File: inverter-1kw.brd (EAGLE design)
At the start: 96.4 x 87.3 mm, 240 parts, among them IC1 LMV358MMX, IC2 LMV358MMX, U1 ACS712, U4 ACS712, U5 SI8230, U6 SI8230, U7 ACS712, X1 GMSTBV3, X2 MSTBV2

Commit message: planler yapıldı tekrar
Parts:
- moved R44 77.4 mm to (20.4, 15.6)
- moved C2 10.7 mm to (29.7, 38.7)
- moved C7 7.79 mm to (35.6, 27.3)
- moved C3 7.74 mm to (35.5, 32.6)
- moved C5 7.62 mm to (35.5, 29.9)
- moved TP20 2.01 mm to (41.2, 18.7)
- moved R7 1.18 mm to (35.9, 22.2)
- moved R6 1.16 mm to (38.9, 22.2)
- moved R5 1.14 mm to (41.9, 22.2)
- moved R74 0.48 mm to (6.38, 62.2)
- moved R72 0.47 mm to (9.11, 62.2)
- moved R68 0.45 mm to (9.93, 66.5)
- moved R2 0.42 mm to (38.8, 16.6)
- moved R3 0.41 mm to (35.8, 16.6)
- moved R1 0.38 mm to (41.9, 16.6)
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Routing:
- net VB_FILTER: track 26.2 -> 2.54 mm
- net VA_OUT: track 18.9 -> 1.30 mm
- net VG1_P: track 14.8 -> 26.8 mm, vias 0 -> 2
- net VIN: track 27.8 -> 21.7 mm, vias 12 -> 18
- net AGND: track 93.0 -> 86.9 mm, vias 56 -> 54
- net DGND: track 146.7 -> 148.6 mm, vias 16 -> 17
- net N$79: track 7.63 -> 6.63 mm
- net SW_LEG_A: track 24.4 -> 24.1 mm, vias 6 -> 20
- net VB_OUT: vias 1 -> 9
- net SW_LEG_B: vias 6 -> 7
- added copper zone on layer 1, net SW_LEG_B
- added copper zone on layer 16, net VB_FILTER

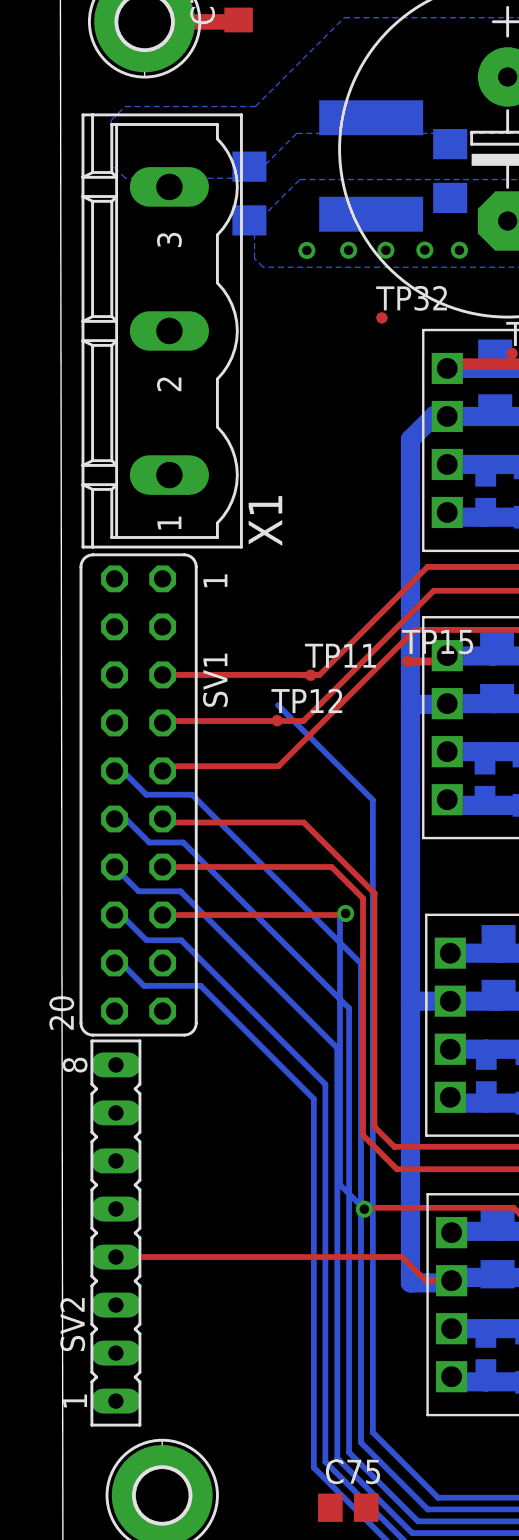
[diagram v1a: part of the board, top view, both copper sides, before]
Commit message: Kontrol karti soketi SMD yapildi, guc giris soketi ve guc-karti soketi bottom-layer'a alindi.
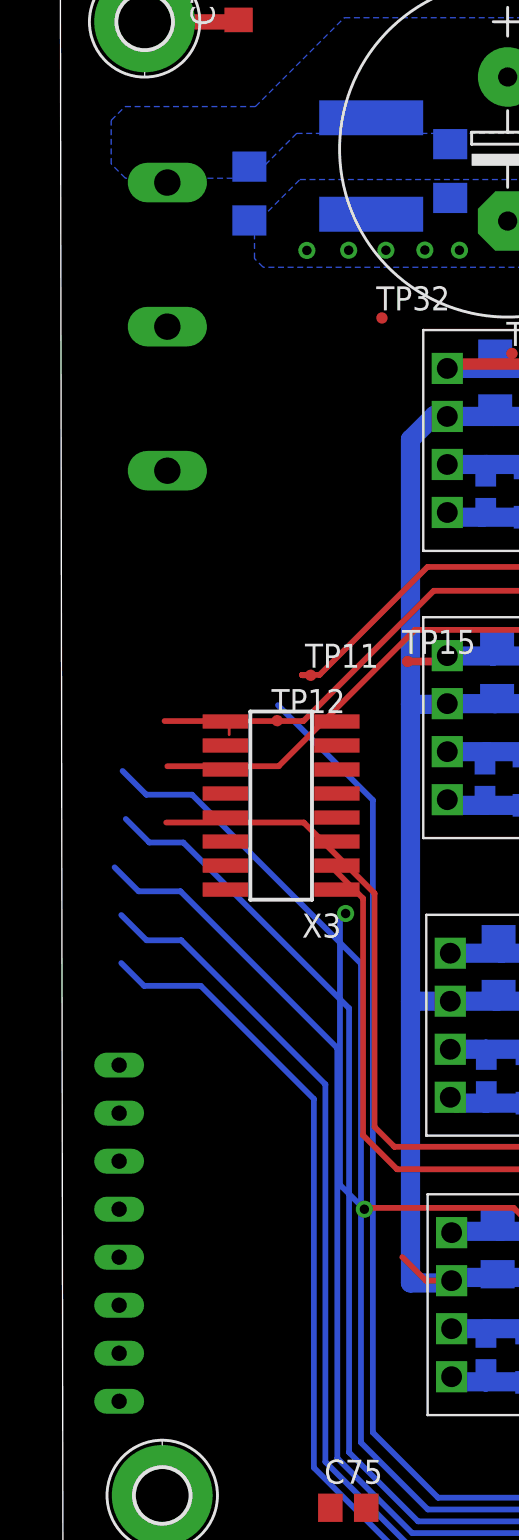
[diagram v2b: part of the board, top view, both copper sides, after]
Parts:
- removed SV1: (no value), con-lsta:FE10-2
- added X3: 1365-16, con-leotronics:1365-16
- moved X1 0.25 mm to (-26.4, 75.3), flipped to the bottom, turned to 270 degrees
- moved SV2 0.17 mm to (-29.0, 27.4), flipped to the bottom
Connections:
- removed net N$38: SV1.8
- removed net RELAY1: SV1.2
- removed net RELAY2: SV1.4
- net +3V3: now also X3.2; no longer SV1.17
- net +5V: no longer SV1.19
- net DGND: now also X3.1; no longer SV1.20
- net DRV1_EN: now also X3.9; no longer SV1.9
- net DRV2_EN: now also X3.3; no longer SV1.15
- net G11_PWM: now also X3.13; no longer SV1.5
- net G12_PWM: now also X3.11; no longer SV1.7
- net G13_PWM: now also X3.7; no longer SV1.11
- net G14_PWM: now also X3.5; no longer SV1.13
- net IA_SENS: now also X3.8; no longer SV1.14
- net IB_SENS: now also X3.4; no longer SV1.18
- net IIN_SENS: now also X3.15; no longer SV1.3
- net VA_SENS: now also X3.10; no longer SV1.12
- net VB_SENS: now also X3.6; no longer SV1.16
- net VIN_SENS: now also X3.16; no longer SV1.1
- net VIN_SENS_DIFF: now also X3.14; no longer SV1.6
- net VOUT_SENS_DIFF: now also X3.12; no longer SV1.10
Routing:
- net PE: track 1.94 -> 17.3 mm
- net VDD: track 93.5 -> 78.4 mm
- net DRV2_EN: track 48.7 -> 39.1 mm
- net G14_PWM: track 43.7 -> 34.8 mm
- net G11_PWM: track 33.6 -> 26.3 mm
- net G12_PWM: track 32.6 -> 33.3 mm
- net VA_SENS: track 164.0 -> 163.4 mm

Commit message: Planeler tamamlandı.
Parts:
- moved TP32 76.9 mm to (61.7, 71.7)
- moved TP14 39.5 mm to (31.8, 22.6)
- moved TP11 38.3 mm to (16.0, 41.1)
- moved TP12 38.0 mm to (14.4, 39.7)
- moved TP21 33.7 mm to (80.3, 15.2)
- moved SV2 33.6 mm to (4.12, 21.7)
- moved C76 33.5 mm to (9.51, 83.1), turned to 270 degrees
- moved TP28 33.3 mm to (33.4, 62.1)
- moved C10 33.2 mm to (87.5, 21.6)
- moved R21 33.2 mm to (85.5, 21.6)
- moved C13 33.2 mm to (74.5, 12.1)
- moved C15 33.2 mm to (74.5, 8.65)
- moved C17 33.2 mm to (87.5, 56.2)
- moved C38 33.2 mm to (78.0, 6.36)
- moved C5 33.2 mm to (67.5, 21.2)
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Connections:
- net PE: now also X1.3; no longer X1.1
- net VSUPPLY+: now also X1.1; no longer X1.3
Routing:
- net +3V3: track 7.94 -> 273.1 mm, vias 1 -> 8
- net PE: track 17.3 -> 259.8 mm, vias 0 -> 1
- net VIN_SENS: track 2.23 -> 84.4 mm, vias 0 -> 1
- net AGND: track 86.9 -> 153.7 mm, vias 54 -> 62
- net IIN_SENS: track 6.73 -> 39.3 mm
- net VDD: track 78.4 -> 92.8 mm
- net G13_PWM: track 46.2 -> 33.5 mm
- net G11_PWM: track 26.3 -> 35.9 mm
- net N$42: track 0.00 -> 6.64 mm
- net VB_OUT: track 7.85 -> 14.4 mm
- net VA_OUT: track 1.30 -> 7.68 mm, vias 0 -> 1
- net VB_SENS: track 153.6 -> 159.3 mm, vias 2 -> 4
- net N$41: track 0.00 -> 5.35 mm
- net VOUT_SENS_DIFF: track 130.1 -> 125.8 mm, vias 1 -> 2
- net IB_SENS: track 140.3 -> 144.3 mm, vias 1 -> 2
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- added copper zone on layer 15, net +5V

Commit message: İyileştirmeler yapıldı
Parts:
- moved C8 6.51 mm to (67.4, 59.2)
- moved C4 6.51 mm to (67.4, 64.9)
- moved C6 6.51 mm to (67.4, 61.9)
- moved TP34 5.56 mm to (18.3, 64.7)
- moved TP33 5.23 mm to (33.1, 69.2), turned to 90 degrees
- moved C1 2.31 mm to (61.8, 52.7)
- moved TP22 1.01 mm to (86.1, 5.34)
- moved TP14 0.61 mm to (32.1, 23.1)
- moved TP5 0.60 mm to (45.1, 54.1)
- moved TP8 0.42 mm to (46.2, 17.4)
- moved TP12 0.40 mm to (14.8, 39.8)
- moved C12 0.39 mm to (85.4, 12.1)
- moved C21 0.39 mm to (85.4, 8.67)
- moved C22 0.35 mm to (87.2, 8.67)
- moved R17 0.35 mm to (87.2, 12.1)
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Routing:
- net AGND: track 153.7 -> 169.4 mm, vias 62 -> 86
- net VA_FILTER: track 28.0 -> 16.1 mm
- net IIN_SENS: track 39.3 -> 46.6 mm, vias 1 -> 2
- net VG2_M: track 22.9 -> 15.7 mm
- net SW_LEG_B: track 9.58 -> 16.6 mm, vias 7 -> 6
- net VG3_M: track 18.9 -> 24.5 mm, vias 0 -> 1
- net VG2_P: track 22.8 -> 28.0 mm, vias 2 -> 3
- net DGND: track 147.6 -> 152.2 mm
- net VG1_M: track 19.8 -> 23.9 mm, vias 0 -> 1
- net VG4_M: track 20.8 -> 18.0 mm, vias 0 -> 1
- net N$4: track 0.00 -> 2.26 mm
- net VIN: track 21.7 -> 19.5 mm, vias 18 -> 23
- net +3V3: track 273.1 -> 275.2 mm
- net N$35: track 2.91 -> 4.95 mm
- net G11_PWM: track 35.9 -> 37.8 mm
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- added copper zone on layer 16, net VA_FILTER

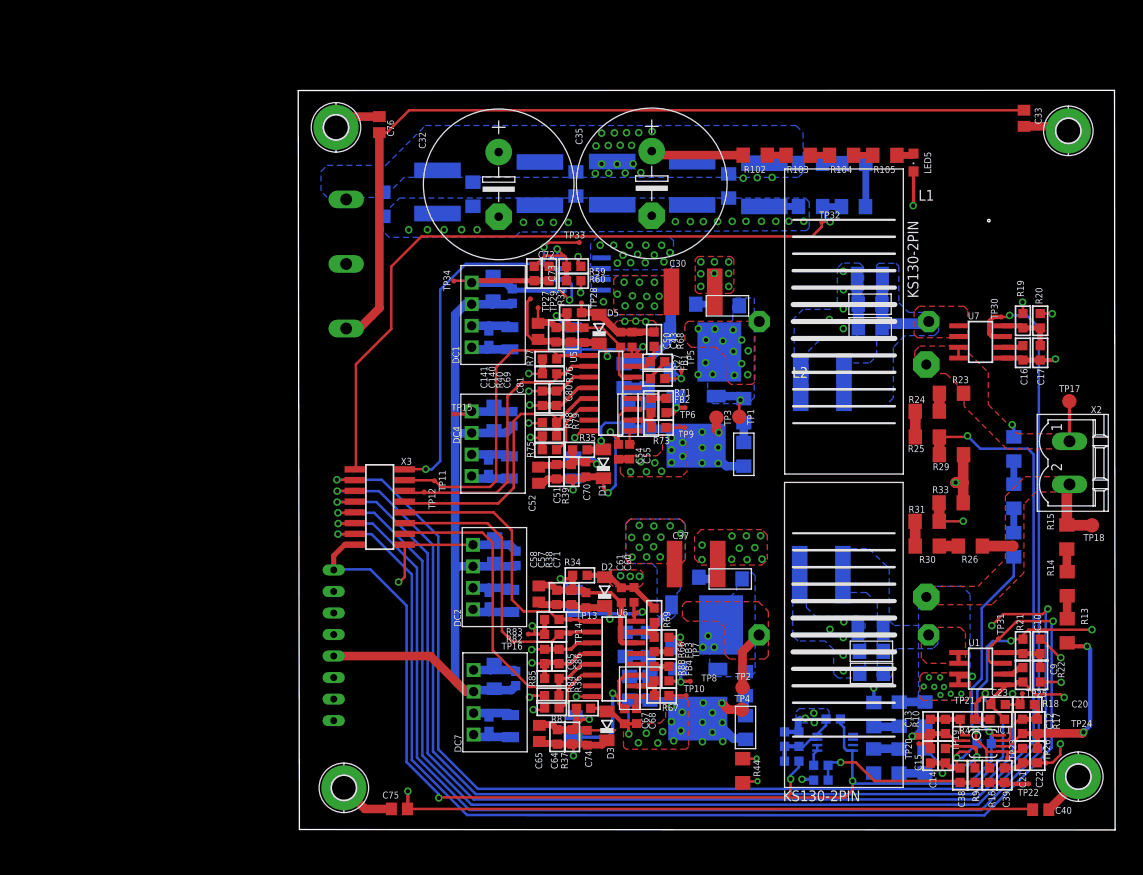
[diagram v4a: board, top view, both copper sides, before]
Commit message: 3v3 kalınlaştırıldı, soket GND si plane yapıldı
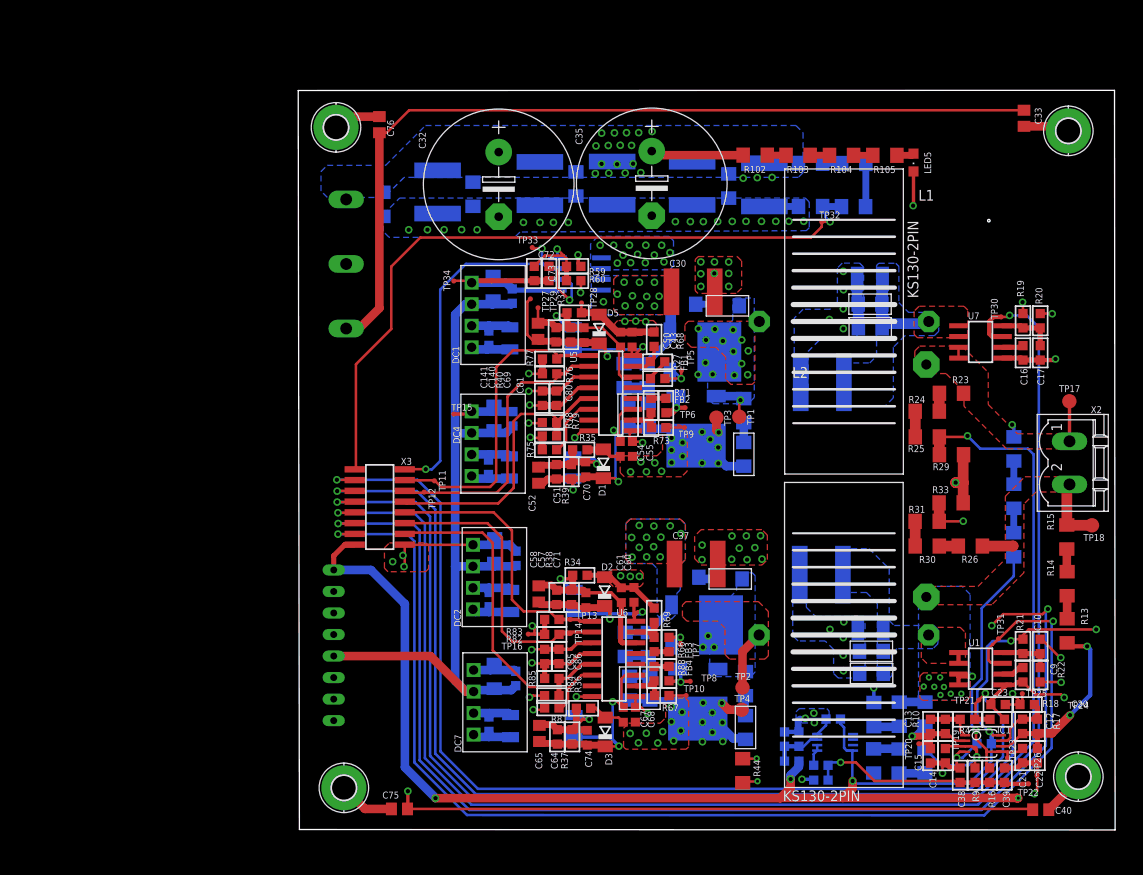
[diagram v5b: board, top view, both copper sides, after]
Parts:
- moved TP33 5.58 mm to (27.6, 68.6)
- moved TP24 2.19 mm to (91.1, 13.5)
- moved TP26 1.85 mm to (87.1, 6.31)
- moved D3 0.75 mm to (36.2, 11.5)
- moved C55 0.47 mm to (39.4, 44.9)
- moved C54 0.39 mm to (37.9, 44.9)
- moved C67 0.22 mm to (38.3, 13.5)
- moved C68 0.21 mm to (39.7, 13.5)
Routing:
- net +3V3: track 275.2 -> 321.9 mm, vias 8 -> 9
- net AGND: track 169.4 -> 153.8 mm, vias 86 -> 85
- net VG2_M: track 15.7 -> 23.0 mm, vias 1 -> 2
- net VG4_M: track 18.0 -> 23.6 mm, vias 1 -> 2
- net IIN_SENS: track 46.6 -> 43.2 mm
- net N$23: track 26.7 -> 23.6 mm
- net VB_SENS: track 159.4 -> 162.2 mm
- net IA_SENS: track 174.5 -> 177.2 mm
- net DGND: track 152.2 -> 149.5 mm, vias 18 -> 20
- net VA_SENS: track 163.5 -> 166.3 mm
- net VOUT_SENS_DIFF: track 124.9 -> 127.5 mm
- net IB_SENS: track 143.2 -> 145.7 mm
- net VIN_SENS_DIFF: track 126.0 -> 128.4 mm
- net VG2_P: track 28.0 -> 26.1 mm
- added copper zone on layer 1, net DGND

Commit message: R3'un eksik baglantisi yapildi. 8'li besleme karti giris gerilimi baglantisi yapildi.
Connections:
- removed net POWER_IN: SV2.1
- removed net SUPPLY+: R3.1
- net VSUPPLY+: now also R3.1, SV2.1
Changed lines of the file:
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@@
 <drawing>
 <settings>
-<setting alwaysvectorfont="yes"/>
+<setting alwaysvectorfont="no"/>
 <setting verticaltext="up"/>
 </settings>
@@
 <via x="35.56" y="68.9" extent="1-16" drill="0.5"/>
 <contactref element="X1" pad="1"/>
+<contactref element="R3" pad="1"/>
+<contactref element="SV2" pad="1"/>
+<wire x1="55.85" y1="76.9" x2="58.968" y2="78.565" width="0" layer="19" extent="16-16"/>
+<wire x1="54.1" y1="76.87" x2="55.85" y2="76.9" width="0" layer="19" extent="1-1"/>
+<wire x1="52.44" y1="76.81" x2="54.1" y2="76.87" width="0" layer="19" extent="1-1"/>
+<wire x1="50.73" y1="77.312" x2="52.44" y2="76.81" width="0" layer="19" extent="16-16"/>
+<wire x1="54.94" y1="78.575" x2="55.85" y2="76.9" width="0" layer="19" extent="16-16"/>
+<wire x1="52.438" y1="79.53" x2="54.94" y2="78.575" width="0" layer="19" extent="1-16"/>
+<wire x1="41.69" y1="82.32" x2="41.65" y2="80.005" width="0" layer="19" extent="1-1"/>
+<wire x1="40.11" y1="82.19" x2="41.69" y2="82.32" width="0" layer="19" extent="1-1"/>
+<wire x1="38.67" y1="82.18" x2="40.11" y2="82.19" width="0" layer="19" extent="1-1"/>
+<wire x1="37.25" y1="82.16" x2="38.67" y2="82.18" width="0" layer="19" extent="1-1"/>
+<wire x1="35.74" y1="82.13" x2="37.25" y2="82.16" width="0" layer="19" extent="1-1"/>
+<wire x1="37.93" y1="80.7" x2="37.25" y2="82.16" width="0" layer="19" extent="1-1"/>
+<wire x1="39.27" y1="80.68" x2="37.93" y2="80.7" width="0" layer="19" extent="1-1"/>
+<wire x1="36.52" y1="80.67" x2="37.93" y2="80.7" width="0" layer="19" extent="1-1"/>
+<wire x1="35.07" y1="80.62" x2="36.52" y2="80.67" width="0" layer="19" extent="1-1"/>
+<wire x1="36.98" y1="78.775" x2="36.52" y2="80.67" width="0" layer="19" extent="16-16"/>
+<wire x1="37.56" y1="78.46" x2="36.98" y2="78.775" width="0" layer="19" extent="16-16"/>
+<wire x1="35.73" y1="78.5" x2="36.98" y2="78.775" width="0" layer="19" extent="16-16"/>
+<wire x1="34.99" y1="77.37" x2="35.73" y2="78.5" width="0" layer="19" extent="1-1"/>
+<wire x1="36.58" y1="77.41" x2="35.73" y2="78.5" width="0" layer="19" extent="1-1"/>
+<wire x1="38.52" y1="77.42" x2="37.56" y2="78.46" width="0" layer="19" extent="1-1"/>
+<wire x1="39.45" y1="78.52" x2="38.52" y2="77.42" width="0" layer="19" extent="1-1"/>
+<wire x1="40.36" y1="77.47" x2="39.45" y2="78.52" width="0" layer="19" extent="1-1"/>
+<wire x1="32.7" y1="77.552" x2="34.99" y2="77.37" width="0" layer="19" extent="16-16"/>
+<wire x1="28.45" y1="78.725" x2="32.7" y2="77.552" width="0" layer="19" extent="16-16"/>
+<wire x1="46.42" y1="78.755" x2="50.73" y2="77.312" width="0" layer="19" extent="16-16"/>
+<wire x1="23.59" y1="79.895" x2="28.45" y2="78.725" width="0" layer="19" extent="16-16"/>
+<wire x1="20.55" y1="76.342" x2="23.59" y2="79.895" width="0" layer="19" extent="16-16"/>
+<wire x1="16.37" y1="77.735" x2="20.55" y2="76.342" width="0" layer="19" extent="16-16"/>
+<wire x1="9.93" y1="75.152" x2="16.37" y2="77.735" width="0" layer="19" extent="16-16"/>
+<wire x1="5.59" y1="74.31" x2="9.93" y2="75.152" width="0" layer="19" extent="16-16"/>
+<wire x1="35.56" y1="68.9" x2="34.99" y2="77.37" width="0" layer="19" extent="1-1"/>
+<wire x1="35.72" y1="67.415" x2="35.56" y2="68.9" width="0" layer="19" extent="16-16"/>
+<wire x1="35.72" y1="66.145" x2="35.72" y2="67.415" width="0" layer="19" extent="16-16"/>
+<wire x1="37.16" y1="68.9" x2="35.56" y2="68.9" width="0" layer="19" extent="1-1"/>
+<wire x1="38.26" y1="67.74" x2="37.16" y2="68.9" width="0" layer="19" extent="1-1"/>
+<wire x1="37.59" y1="66.79" x2="38.26" y2="67.74" width="0" layer="19" extent="1-1"/>
+<wire x1="39.16" y1="66.84" x2="38.26" y2="67.74" width="0" layer="19" extent="1-1"/>
+<wire x1="39.98" y1="67.83" x2="39.16" y2="66.84" width="0" layer="19" extent="1-1"/>
+<wire x1="40.89" y1="66.83" x2="39.98" y2="67.83" width="0" layer="19" extent="1-1"/>
+<wire x1="39.02" y1="68.91" x2="38.26" y2="67.74" width="0" layer="19" extent="1-1"/>
+<wire x1="41.95" y1="67.74" x2="40.89" y2="66.83" width="0" layer="19" extent="1-1"/>
+<wire x1="43.09" y1="66.94" x2="41.95" y2="67.74" width="0" layer="19" extent="1-1"/>
+<wire x1="43.8" y1="68.03" x2="43.09" y2="66.94" width="0" layer="19" extent="1-1"/>
+<wire x1="42.82" y1="68.9" x2="43.8" y2="68.03" width="0" layer="19" extent="1-1"/>
+<wire x1="40.95" y1="68.9" x2="39.98" y2="67.83" width="0" layer="19" extent="1-1"/>
+<wire x1="4.12" y1="12.8" x2="5.59" y2="74.31" width="0" layer="19" extent="1-1"/>
+<wire x1="67.83" y1="6.593" x2="4.12" y2="12.8" width="0" layer="19" extent="16-16"/>
 </signal>
 <signal name="N$69">
@@
 <wire x1="4.52915625" y1="39.884" x2="4.56015625" y2="39.915" width="0.3048" layer="1"/>
 </signal>
-<signal name="POWER_IN">
-<contactref element="SV2" pad="1"/>
-</signal>
 <signal name="N$54">
 <contactref element="R102" pad="1"/>
@@
 <wire x1="32.32" y1="28.32" x2="32.19" y2="28.19" width="0.4064" layer="1"/>
 </signal>
-<signal name="SUPPLY+">
-<contactref element="R3" pad="1"/>
-</signal>
 <signal name="N$40">

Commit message: Düzenlemeler yapıldı
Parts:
- moved TP9 2.94 mm to (43.0, 45.9)
- moved TP16 0.97 mm to (26.1, 23.2)
- moved C57 0.70 mm to (30.4, 28.0)
- moved R34 0.59 mm to (33.1, 30.5)
- moved C58 0.55 mm to (28.3, 28.3)
- moved R38 0.54 mm to (32.2, 27.9)
- moved R74 0.48 mm to (38.4, 54.0)
- moved R72 0.48 mm to (41.1, 54.0)
- moved R82 0.44 mm to (29.9, 23.4)
- moved R83 0.42 mm to (29.9, 25.2)
- moved TP7 0.31 mm to (45.1, 21.4)
- moved TP5 0.30 mm to (45.1, 54.4)
- moved TP6 0.29 mm to (45.8, 49.6)
- moved C86 0.17 mm to (30.8, 20.5)
- moved C50 0.16 mm to (37.9, 57.9)
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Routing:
- net VSUPPLY+: track 11.0 -> 143.3 mm, vias 32 -> 38
- net AGND: track 153.8 -> 165.8 mm, vias 85 -> 84
- net SW_LEG_A: track 23.6 -> 27.8 mm, vias 18 -> 21
- net +3V3: track 321.9 -> 323.8 mm
- net VREF: track 26.7 -> 28.5 mm
- net +5V: track 28.6 -> 30.4 mm
- net N$79: track 6.63 -> 7.61 mm
- net DRV2_EN: track 39.8 -> 40.8 mm
- net VDD: track 92.8 -> 93.7 mm
- net N$35: track 4.95 -> 5.84 mm
- net VG1_P: track 27.5 -> 28.3 mm
- net VG4_P: track 27.8 -> 27.0 mm
- net VG4_M: track 23.6 -> 24.3 mm
- net VG2_M: track 23.0 -> 23.7 mm
- net SW_LEG_B: track 16.6 -> 17.2 mm
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- added copper zone on layer 2, net VSUPPLY+

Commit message: son hali
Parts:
- moved D3 0.10 mm to (36.3, 11.4)
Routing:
- net VG4_P: track 27.0 -> 28.1 mm
